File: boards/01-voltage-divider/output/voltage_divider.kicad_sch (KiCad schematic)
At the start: 4 parts, among them J1 IN, J2 OUT

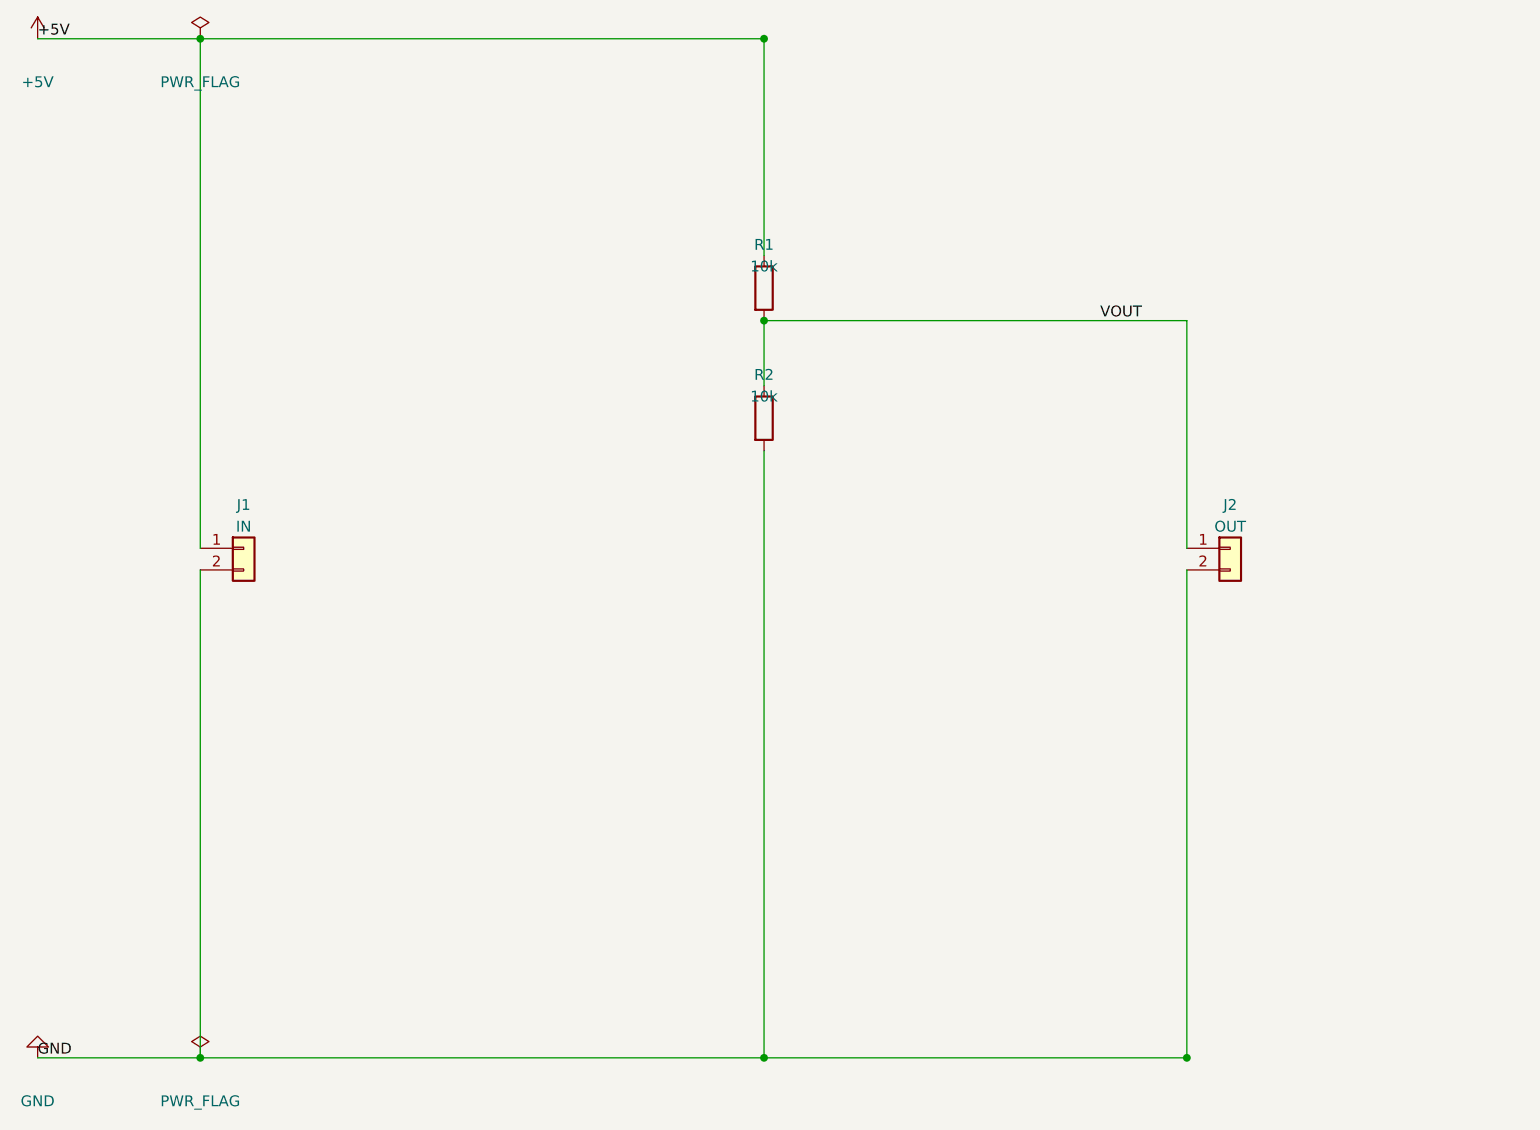
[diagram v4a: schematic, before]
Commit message: fix(footprint): use R_0805 in default profile and fix board 02 U1 footprint (#1545)
Change the default footprint selector profile to map all resistor values
to R_0805_2012Metric instead of R_0402_1005Metric, matching what the PCB
generation scripts actually place. Also fix board 02's U1 schematic
footprint from PinHeader_1x08 to DIP-8_W7.62mm to match its PCB footprint.

Regenerate output files for boards 01 and 02 to reflect corrected footprints.

Co-authored-by: Claude Opus 4.6 <noreply@anthropic.com>
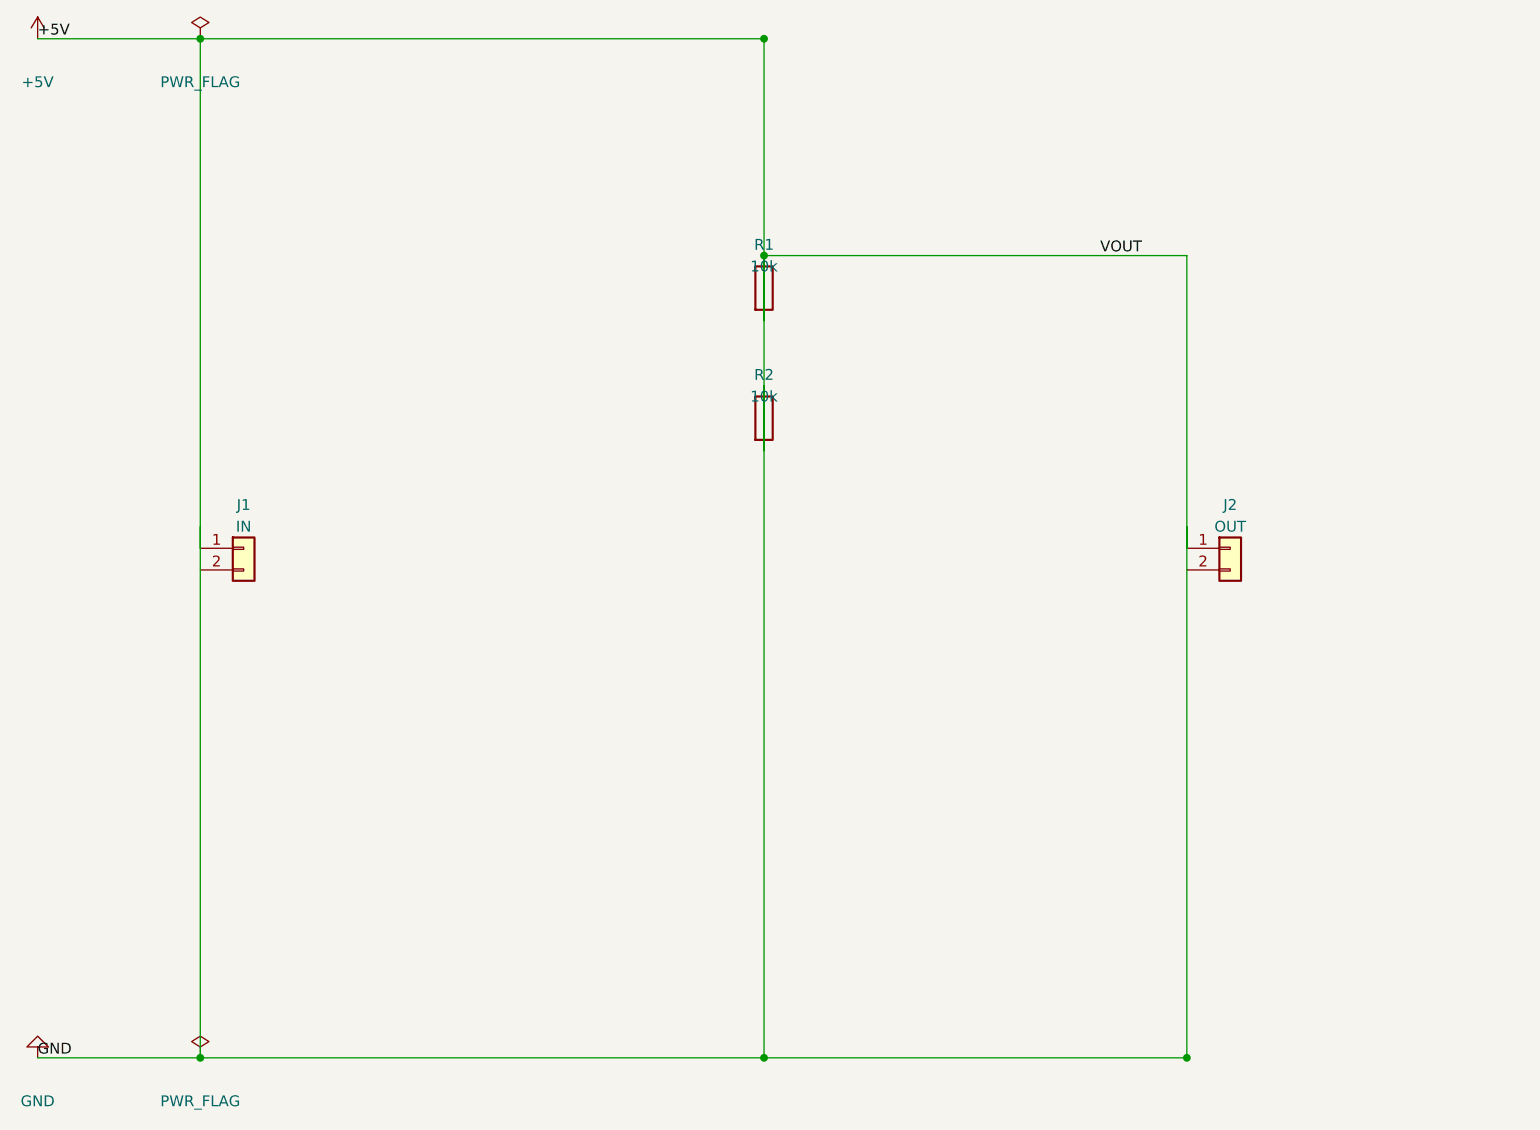
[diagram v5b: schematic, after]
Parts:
- R1, R2: footprint Resistor_SMD:R_0402_1005Metric -> Resistor_SMD:R_0805_2012Metric
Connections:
- net VOUT is gone; now on net +5V: J2.1 (Pin_1), R1.2, R2.1
- net +5V: now also R2.2
- removed net GND: J1.2 (Pin_2), J2.2 (Pin_2), R2.2
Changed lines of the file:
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@@
     (instances
       (project "project"
-        (path "/f248c599-1edb-428b-92f1-1714e73d748a" (reference "J1") (unit 1)
+        (path "/c9ee47c7-1601-47a4-949b-2f918498a9b4" (reference "J1") (unit 1)
         )
       )
@@
       )
     )
-    (property "Footprint" "Resistor_SMD:R_0402_1005Metric"
+    (property "Footprint" "Resistor_SMD:R_0805_2012Metric"
       (at 110.49 59.69 0)
       (effects
@@
     (instances
       (project "project"
-        (path "/f248c599-1edb-428b-92f1-1714e73d748a" (reference "R1") (unit 1)
+        (path "/c9ee47c7-1601-47a4-949b-2f918498a9b4" (reference "R1") (unit 1)
         )
       )
@@
       )
     )
-    (property "Footprint" "Resistor_SMD:R_0402_1005Metric"
+    (property "Footprint" "Resistor_SMD:R_0805_2012Metric"
       (at 110.49 74.93 0)
       (effects
@@
     (instances
       (project "project"
-        (path "/f248c599-1edb-428b-92f1-1714e73d748a" (reference "R2") (unit 1)
+        (path "/c9ee47c7-1601-47a4-949b-2f918498a9b4" (reference "R2") (unit 1)
         )
       )
@@
     (instances
       (project "project"
-        (path "/f248c599-1edb-428b-92f1-1714e73d748a" (reference "J2") (unit 1)
+        (path "/c9ee47c7-1601-47a4-949b-2f918498a9b4" (reference "J2") (unit 1)
         )
       )
@@
     (instances
       (project "project"
-        (path "/f248c599-1edb-428b-92f1-1714e73d748a" (reference "#PWR01") (unit 1)
+        (path "/c9ee47c7-1601-47a4-949b-2f918498a9b4" (reference "#PWR01") (unit 1)
         )
       )
@@
     (instances
       (project "project"
-        (path "/f248c599-1edb-428b-92f1-1714e73d748a" (reference "#PWR02") (unit 1)
+        (path "/c9ee47c7-1601-47a4-949b-2f918498a9b4" (reference "#PWR02") (unit 1)
         )
       )
@@
     (instances
       (project "project"
-        (path "/f248c599-1edb-428b-92f1-1714e73d748a" (reference "#PWR03") (unit 1)
+        (path "/c9ee47c7-1601-47a4-949b-2f918498a9b4" (reference "#PWR03") (unit 1)
         )
       )
@@
     (instances
       (project "project"
-        (path "/f248c599-1edb-428b-92f1-1714e73d748a" (reference "#PWR04") (unit 1)
+        (path "/c9ee47c7-1601-47a4-949b-2f918498a9b4" (reference "#PWR04") (unit 1)
         )
       )
@@
   )
   (wire
-    (pts (xy 44.45 92.71) (xy 44.45 149.86))
-    (stroke
-      (width 0)
-      (type default)
-    )
-  )
-  (wire
-    (pts (xy 110.49 55.88) (xy 110.49 30.48))
-    (stroke
-      (width 0)
-      (type default)
-    )
-  )
-  (wire
-    (pts (xy 110.49 63.5) (xy 110.49 71.12))
-    (stroke
-      (width 0)
-      (type default)
-    )
-  )
-  (wire
-    (pts (xy 110.49 78.74) (xy 110.49 149.86))
-    (stroke
-      (width 0)
-      (type default)
-    )
-  )
-  (wire
-    (pts (xy 110.49 63.5) (xy 160.02 63.5))
-    (stroke
-      (width 0)
-      (type default)
-    )
-  )
-  (wire
-    (pts (xy 160.02 63.5) (xy 160.02 90.17))
-    (stroke
-      (width 0)
-      (type default)
-    )
-  )
-  (wire
-    (pts (xy 160.02 92.71) (xy 160.02 149.86))
+    (pts (xy 44.45 87.63) (xy 44.45 149.86))
+    (stroke
+      (width 0)
+      (type default)
+    )
+  )
+  (wire
+    (pts (xy 110.49 63.5) (xy 110.49 30.48))
+    (stroke
+      (width 0)
+      (type default)
+    )
+  )
+  (wire
+    (pts (xy 110.49 55.88) (xy 110.49 78.74))
+    (stroke
+      (width 0)
+      (type default)
+    )
+  )
+  (wire
+    (pts (xy 110.49 71.12) (xy 110.49 149.86))
+    (stroke
+      (width 0)
+      (type default)
+    )
+  )
+  (wire
+    (pts (xy 110.49 55.88) (xy 160.02 55.88))
+    (stroke
+      (width 0)
+      (type default)
+    )
+  )
+  (wire
+    (pts (xy 160.02 55.88) (xy 160.02 90.17))
+    (stroke
+      (width 0)
+      (type default)
+    )
+  )
+  (wire
+    (pts (xy 160.02 87.63) (xy 160.02 149.86))
     (stroke
       (width 0)
@@
   )
   (junction
-    (at 110.49 63.5)
+    (at 110.49 55.88)
     (diameter 0)
   )
@@
   )
   (label "VOUT"
-    (at 149.86 63.5 0)
+    (at 149.86 55.88 0)
     (fields_autoplaced yes)
     (effects
@@
   )
   (sheet_instances
-    (path "/f248c599-1edb-428b-92f1-1714e73d748a" (page "1")
-    )
-  )
+    (path "/c9ee47c7-1601-47a4-949b-2f918498a9b4" (page "1")
+    )
+  )
